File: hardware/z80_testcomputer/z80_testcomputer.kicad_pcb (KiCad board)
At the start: 2 copper layers, 95 x 100 mm, 19 parts, among them J2 Conn_02x15_Odd_Even, J3 Conn_01x32, U1 Z84C000XPEG, U2 SRAM_512K8B_DIP_SOP_SOJ, U3 EEPROM_512K8B_DIP

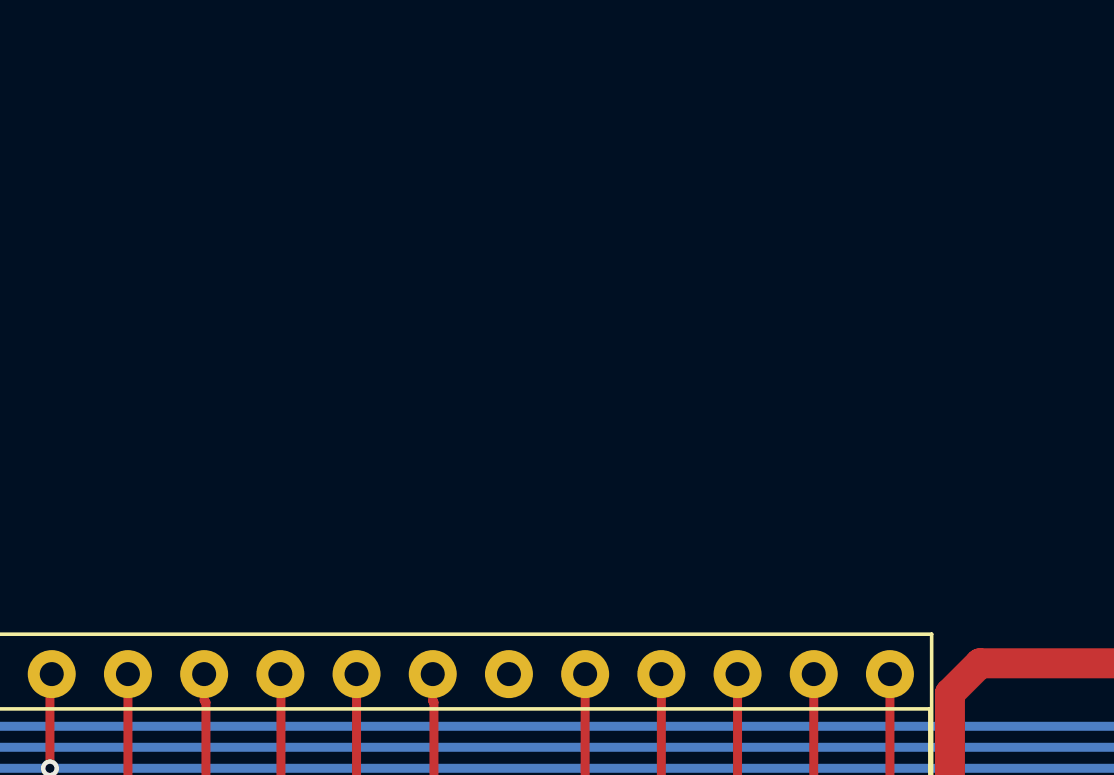
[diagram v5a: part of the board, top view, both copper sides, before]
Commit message: wrong package for 74138, placement on PCB
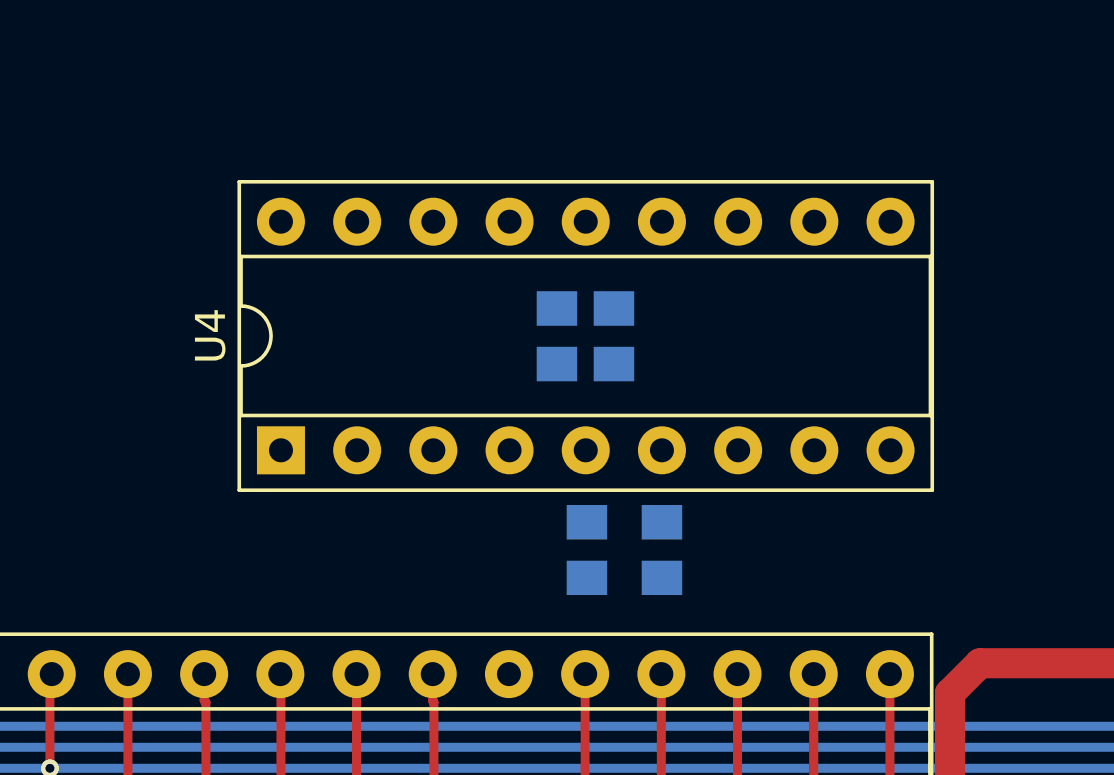
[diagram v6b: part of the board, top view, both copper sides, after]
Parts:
- added C7: 1u, SquantorRcl:C_0805+0603, B.Cu at (165.0, 83.1)
- added C8: 100n, SquantorRcl:C_0805+0603, B.Cu at (163.1, 83.1)
- added R1: 10k, SquantorRcl:C_0805+0603, B.Cu at (164.1, 90.2)
- added R2: 10k, SquantorRcl:C_0805+0603, B.Cu at (166.6, 90.2)
- added U4: 74XX138, Package_DIP:DIP-18_W7.62mm_Socket, F.Cu at (153.9, 86.9)

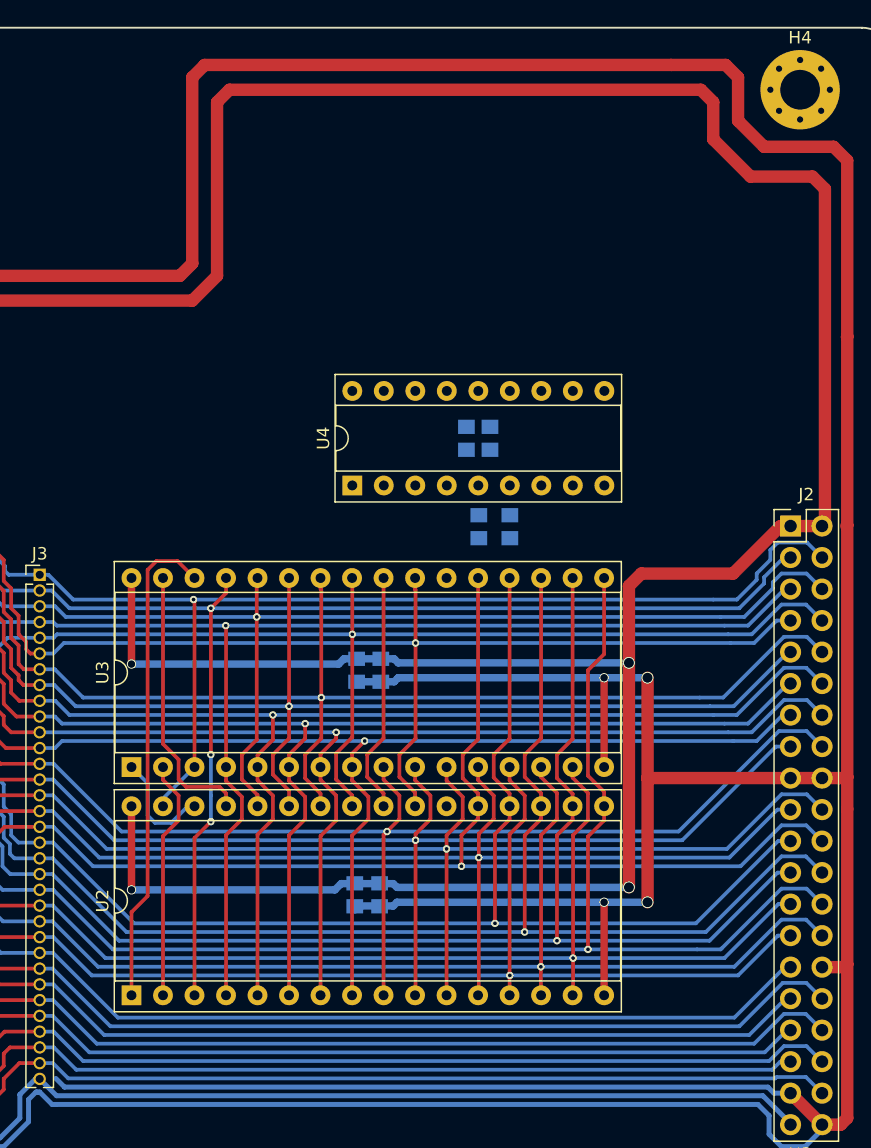
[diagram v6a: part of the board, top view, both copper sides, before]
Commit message: routed IO logic
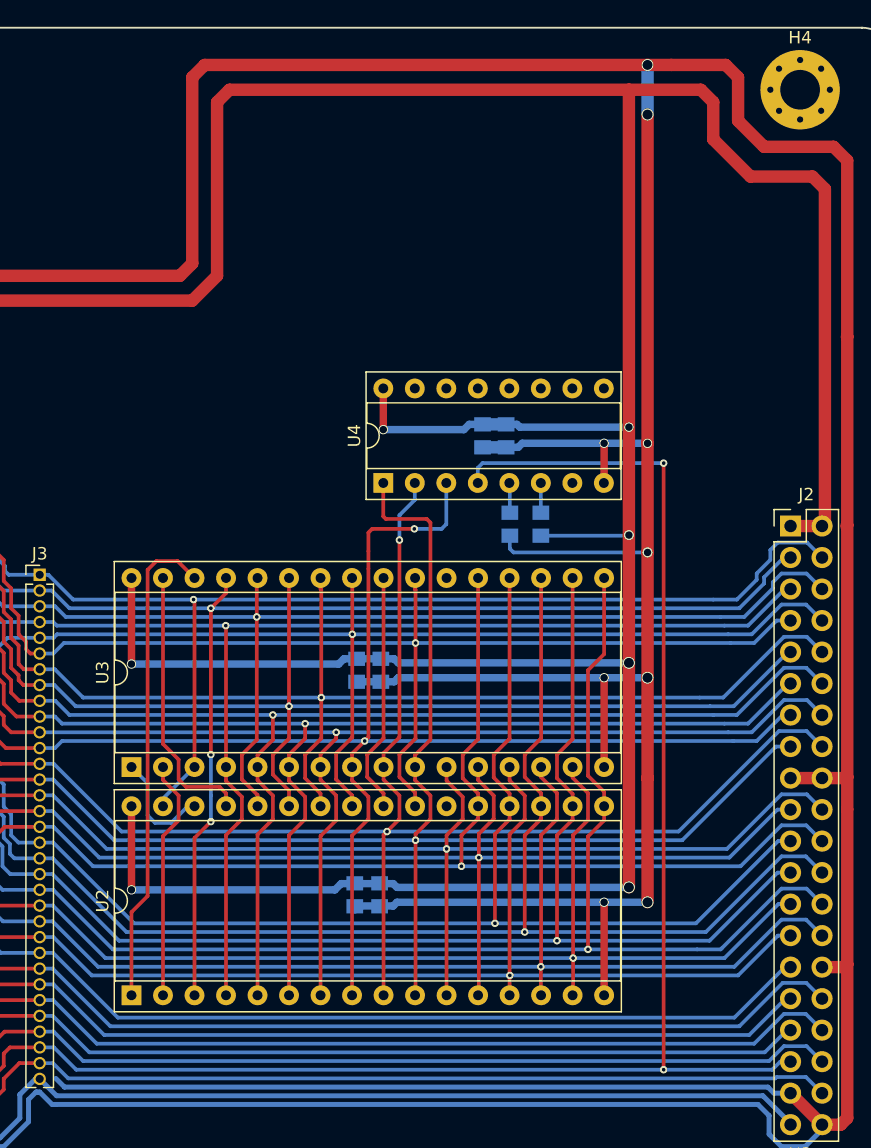
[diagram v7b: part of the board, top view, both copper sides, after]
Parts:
- U4: footprint Package_DIP:DIP-18_W7.62mm_Socket -> Package_DIP:DIP-16_W7.62mm_Socket
- moved U4 2.51 mm to (156.4, 86.7)
- moved R1 2.51 mm to (166.6, 90.0)
- moved R2 2.51 mm to (169.1, 90.0)
- moved C7 1.32 mm to (166.3, 82.9)
- moved C8 1.32 mm to (164.4, 82.9)
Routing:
- net /VSS: track 537.7 -> 604.5 mm, vias 5 -> 10
- net /!IORQ: track 85.1 -> 150.4 mm, vias 0 -> 2
- net /VDD: track 320.1 -> 375.6 mm, vias 5 -> 8
- net /A2: track 90.6 -> 117.5 mm
- net /A4: track 91.0 -> 117.8 mm, vias 1 -> 2
- net /A3: track 95.0 -> 119.0 mm, vias 1 -> 2
- net Net-(R1-Pad1): track 0.00 -> 2.42 mm
- net Net-(R2-Pad1): track 0.00 -> 2.40 mm
